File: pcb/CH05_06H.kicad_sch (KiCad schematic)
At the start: 10 parts

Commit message: Corrections to the coax driver
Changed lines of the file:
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@@
     (effects (font (size 1.27 1.27)) (justify right))
   )
-  (symbol (lib_id "Device:R") (at 96.52 52.07 270)
+  (symbol (lib_id "Device:R") (at 96.52 52.07 270) (unit 1)
     (in_bom yes) (on_board yes)
     (property "Reference" "R?" (id 0) (at 96.52 46.8122 90))
@@
     (pin "2")
   )
-  (symbol (lib_id "Device:R") (at 115.57 69.85 0)
+  (symbol (lib_id "Device:R") (at 115.57 69.85 0) (unit 1)
     (in_bom yes) (on_board yes)
     (property "Reference" "R?" (id 0) (at 117.348 68.6816 0)
@@
     (pin "2")
   )
-  (symbol (lib_id "power:GND") (at 115.57 87.63 0)
+  (symbol (lib_id "power:GND") (at 115.57 87.63 0) (unit 1)
     (in_bom yes) (on_board yes)
     (property "Reference" "#PWR?" (id 0) (at 115.57 93.98 0)
@@
     (pin "1")
   )
-  (symbol (lib_id "Device:R") (at 115.57 82.55 0)
+  (symbol (lib_id "Device:R") (at 115.57 82.55 0) (unit 1)
     (in_bom yes) (on_board yes)
     (property "Reference" "R?" (id 0) (at 117.348 81.3816 0)
@@
     (pin "2")
   )
-  (symbol (lib_id "Device:R") (at 115.57 135.89 0)
+  (symbol (lib_id "Device:R") (at 115.57 135.89 0) (unit 1)
     (in_bom yes) (on_board yes)
     (property "Reference" "R?" (id 0) (at 117.348 134.7216 0)
@@
     (pin "2")
   )
-  (symbol (lib_id "power:GND") (at 115.57 154.94 0)
+  (symbol (lib_id "power:GND") (at 115.57 154.94 0) (unit 1)
     (in_bom yes) (on_board yes)
     (property "Reference" "#PWR?" (id 0) (at 115.57 161.29 0)
@@
     (pin "1")
   )
-  (symbol (lib_id "Device:R") (at 115.57 148.59 0)
+  (symbol (lib_id "Device:R") (at 115.57 148.59 0) (unit 1)
     (in_bom yes) (on_board yes)
     (property "Reference" "R?" (id 0) (at 117.348 147.4216 0)
@@
     (pin "2")
   )
-  (symbol (lib_id "Connector:Conn_Coaxial") (at 115.57 59.69 0)
+  (symbol (lib_id "Connector:Conn_Coaxial") (at 115.57 59.69 0) (unit 1)
     (in_bom yes) (on_board yes)
     (property "Reference" "J?" (id 0) (at 118.11 60.325 0)
@@
     (pin "2")
   )
-  (symbol (lib_id "Connector:Conn_Coaxial") (at 115.57 125.73 0)
+  (symbol (lib_id "Connector:Conn_Coaxial") (at 115.57 125.73 0) (unit 1)
     (in_bom yes) (on_board yes)
     (property "Reference" "J?" (id 0) (at 118.11 126.365 0)
@@
     (pin "2")
   )
-  (symbol (lib_id "Device:R") (at 93.98 118.11 270)
+  (symbol (lib_id "Device:R") (at 93.98 118.11 270) (unit 1)
     (in_bom yes) (on_board yes)
     (property "Reference" "R?" (id 0) (at 93.98 112.8522 90))
@@
     (pin "2")
   )
-  (symbol (lib_id "Transistor_BJT:BC856BS") (at 106.68 118.11 0) (mirror x)
+  (symbol (lib_id "Transistor_BJT:BC856BS") (at 106.68 118.11 0) (mirror x) (unit 1)
     (in_bom yes) (on_board yes)
     (property "Reference" "Q?" (id 0) (at 111.506 119.2784 0)
@@
       (effects (font (size 1.27 1.27)) hide)
     )
-    (pin "3")
-    (pin "4")
-    (pin "5")
+    (pin "1")
+    (pin "2")
+    (pin "6")
   )
-  (symbol (lib_id "Transistor_BJT:BC856BS") (at 106.68 52.07 0) (mirror x)
+  (symbol (lib_id "Transistor_BJT:BC856BS") (at 106.68 52.07 0) (mirror x) (unit 1)
     (in_bom yes) (on_board yes)
     (property "Reference" "Q?" (id 0) (at 111.506 53.2384 0)

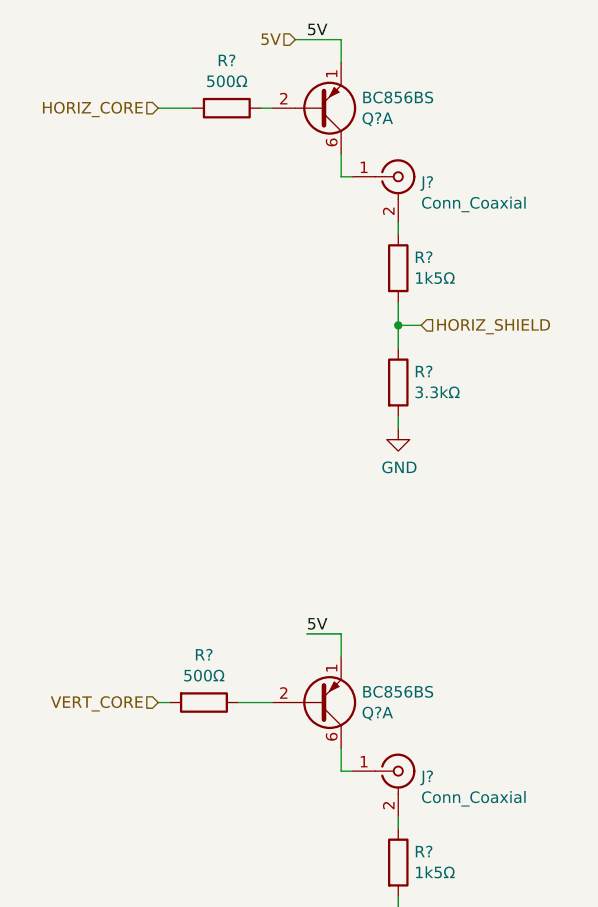
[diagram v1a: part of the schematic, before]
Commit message: Shift register updates - changes the driver from pnp to npn
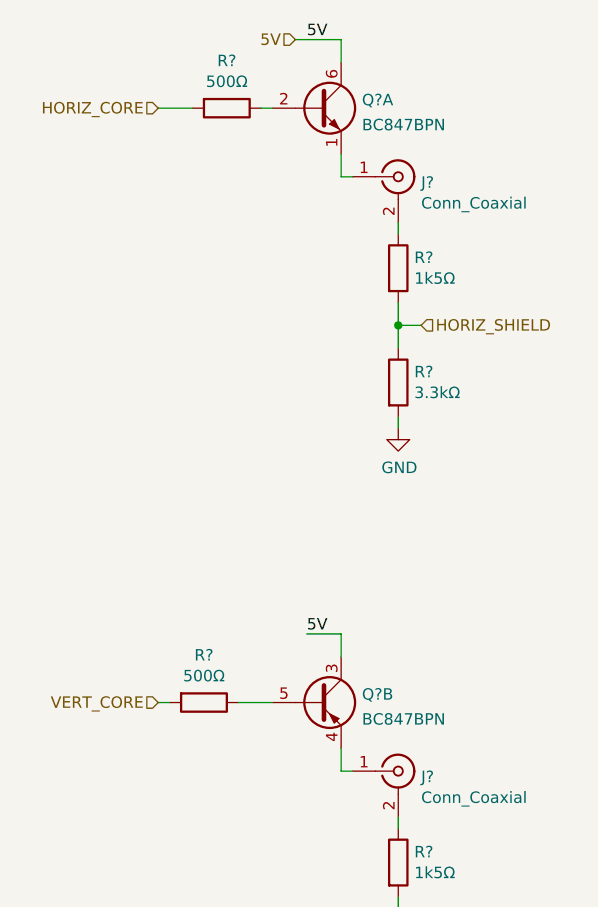
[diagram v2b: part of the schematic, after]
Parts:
- removed Q? (x2): BC856BS, Package_TO_SOT_SMD:SOT-363_SC-70-6, symbol Transistor_BJT:BC856BS
- added Q? (x2): BC847BPN, Package_TO_SOT_SMD:SOT-363_SC-70-6, symbol Transistor_BJT:BC847BPN
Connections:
- net 5V: now also Q?.3 (C2), Q?.6 (C1)
- net at R?.1: now also Q?.2 (B1)
- net at J?.1 (In): now also Q?.1 (E1)
- net at J?.1 (In): now also Q?.4 (E2)
- net at R?.1: now also Q?.5 (B2)
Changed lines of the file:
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@@
     (pin "2")
   )
-  (symbol (lib_id "Transistor_BJT:BC856BS") (at 106.68 118.11 0) (mirror x) (unit 1)
-    (in_bom yes) (on_board yes)
-    (property "Reference" "Q?" (id 0) (at 111.506 119.2784 0)
+  (symbol (lib_id "Transistor_BJT:BC847BPN") (at 106.68 118.11 0) (unit 2)
+    (in_bom yes) (on_board yes) (fields_autoplaced)
+    (property "Reference" "Q?" (id 0) (at 111.5314 117.2015 0)
       (effects (font (size 1.27 1.27)) (justify left))
     )
-    (property "Value" "BC856BS" (id 1) (at 111.506 116.967 0)
+    (property "Value" "BC847BPN" (id 1) (at 111.5314 119.9766 0)
       (effects (font (size 1.27 1.27)) (justify left))
     )
-    (property "Footprint" "Package_TO_SOT_SMD:SOT-363_SC-70-6" (id 2) (at 111.76 120.65 0)
+    (property "Footprint" "Package_TO_SOT_SMD:SOT-363_SC-70-6" (id 2) (at 111.76 115.57 0)
       (effects (font (size 1.27 1.27)) hide)
     )
-    (property "Datasheet" "https://assets.nexperia.com/documents/data-sheet/BC856BS.pdf" (id 3) (at 106.68 118.11 0)
+    (property "Datasheet" "https://assets.nexperia.com/documents/data-sheet/BC847BPN.pdf" (id 3) (at 106.68 118.11 0)
       (effects (font (size 1.27 1.27)) hide)
     )
-    (pin "1")
-    (pin "2")
-    (pin "6")
+    (pin "3")
+    (pin "4")
+    (pin "5")
   )
-  (symbol (lib_id "Transistor_BJT:BC856BS") (at 106.68 52.07 0) (mirror x) (unit 1)
-    (in_bom yes) (on_board yes)
-    (property "Reference" "Q?" (id 0) (at 111.506 53.2384 0)
+  (symbol (lib_id "Transistor_BJT:BC847BPN") (at 106.68 52.07 0) (unit 1)
+    (in_bom yes) (on_board yes) (fields_autoplaced)
+    (property "Reference" "Q?" (id 0) (at 111.5314 51.1615 0)
       (effects (font (size 1.27 1.27)) (justify left))
     )
-    (property "Value" "BC856BS" (id 1) (at 111.506 50.927 0)
+    (property "Value" "BC847BPN" (id 1) (at 111.5314 53.9366 0)
       (effects (font (size 1.27 1.27)) (justify left))
     )
-    (property "Footprint" "Package_TO_SOT_SMD:SOT-363_SC-70-6" (id 2) (at 111.76 54.61 0)
+    (property "Footprint" "Package_TO_SOT_SMD:SOT-363_SC-70-6" (id 2) (at 111.76 49.53 0)
       (effects (font (size 1.27 1.27)) hide)
     )
-    (property "Datasheet" "https://assets.nexperia.com/documents/data-sheet/BC856BS.pdf" (id 3) (at 106.68 52.07 0)
+    (property "Datasheet" "https://assets.nexperia.com/documents/data-sheet/BC847BPN.pdf" (id 3) (at 106.68 52.07 0)
       (effects (font (size 1.27 1.27)) hide)
     )

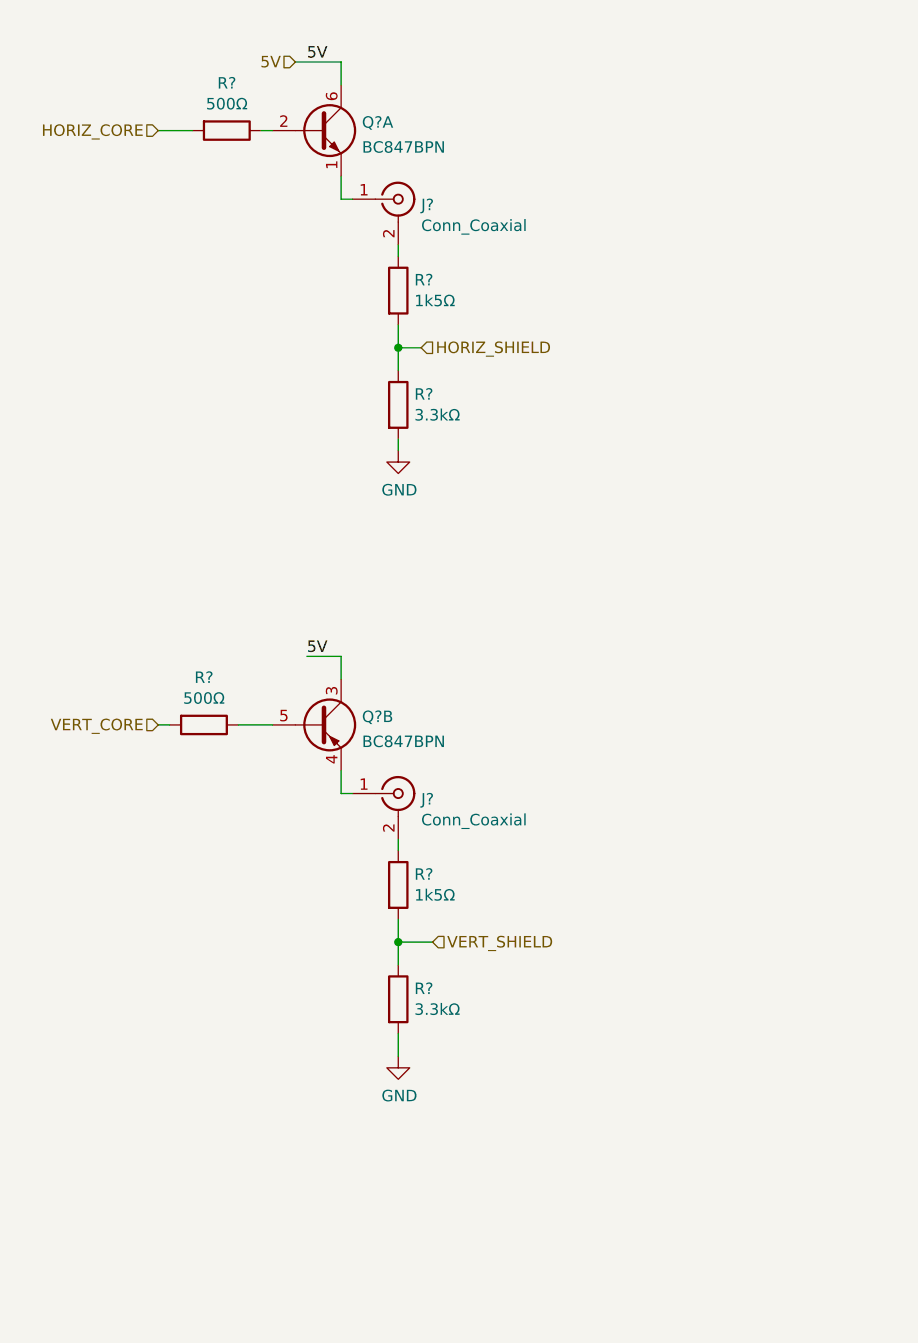
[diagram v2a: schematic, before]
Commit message: Adds line protection
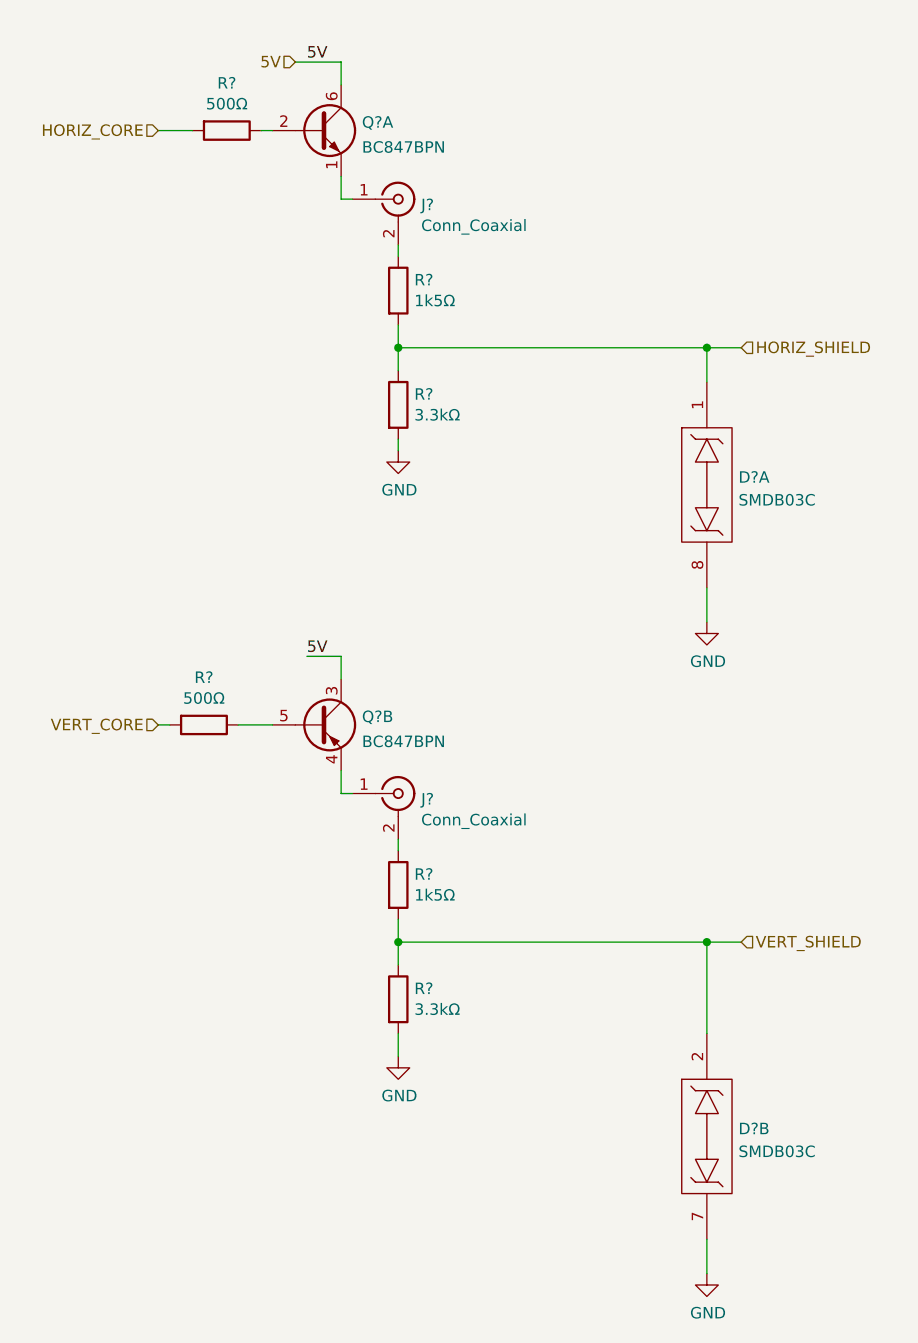
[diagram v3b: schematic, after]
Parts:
- added D? (x2): SMDB03C, Package_SO:SO-8_3.9x4.9mm_P1.27mm, symbol CoaxTester:SMDB03C
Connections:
- net GND: now also D?.7, D?.8
- net HORIZ_SHIELD: now also D?.1
- net VERT_SHIELD: now also D?.2
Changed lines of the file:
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@@
   (junction (at 115.57 76.2) (diameter 0) (color 0 0 0 0)
   )
+  (junction (at 149.86 76.2) (diameter 0) (color 0 0 0 0)
+  )
   (junction (at 115.57 142.24) (diameter 0) (color 0 0 0 0)
   )
+  (junction (at 149.86 142.24) (diameter 0) (color 0 0 0 0)
+  )
   (wire (pts (xy 88.9 118.11) (xy 90.17 118.11))
     (stroke (width 0) (type default) (color 0 0 0 0))
@@
     (stroke (width 0) (type default) (color 0 0 0 0))
   )
-  (wire (pts (xy 115.57 76.2) (xy 118.11 76.2))
+  (wire (pts (xy 115.57 76.2) (xy 149.86 76.2))
     (stroke (width 0) (type default) (color 0 0 0 0))
   )
@@
     (stroke (width 0) (type default) (color 0 0 0 0))
   )
+  (wire (pts (xy 149.86 102.87) (xy 149.86 106.68))
+    (stroke (width 0) (type default) (color 0 0 0 0))
+  )
   (wire (pts (xy 109.22 59.69) (xy 110.49 59.69))
     (stroke (width 0) (type default) (color 0 0 0 0))
@@
     (stroke (width 0) (type default) (color 0 0 0 0))
   )
+  (wire (pts (xy 115.57 142.24) (xy 149.86 142.24))
+    (stroke (width 0) (type default) (color 0 0 0 0))
+  )
   (wire (pts (xy 109.22 110.49) (xy 105.41 110.49))
     (stroke (width 0) (type default) (color 0 0 0 0))
@@
     (stroke (width 0) (type default) (color 0 0 0 0))
   )
+  (wire (pts (xy 149.86 76.2) (xy 153.67 76.2))
+    (stroke (width 0) (type default) (color 0 0 0 0))
+  )
+  (wire (pts (xy 149.86 76.2) (xy 149.86 80.01))
+    (stroke (width 0) (type default) (color 0 0 0 0))
+  )
   (wire (pts (xy 88.9 52.07) (xy 92.71 52.07))
     (stroke (width 0) (type default) (color 0 0 0 0))
@@
     (stroke (width 0) (type default) (color 0 0 0 0))
   )
+  (wire (pts (xy 149.86 142.24) (xy 153.67 142.24))
+    (stroke (width 0) (type default) (color 0 0 0 0))
+  )
+  (wire (pts (xy 149.86 175.26) (xy 149.86 179.07))
+    (stroke (width 0) (type default) (color 0 0 0 0))
+  )
   (wire (pts (xy 100.33 52.07) (xy 101.6 52.07))
     (stroke (width 0) (type default) (color 0 0 0 0))
@@
     (stroke (width 0) (type default) (color 0 0 0 0))
   )
-  (wire (pts (xy 115.57 142.24) (xy 119.38 142.24))
+  (wire (pts (xy 149.86 142.24) (xy 149.86 152.4))
     (stroke (width 0) (type default) (color 0 0 0 0))
   )
@@
     (effects (font (size 1.27 1.27)) (justify left bottom))
   )
-  (hierarchical_label "HORIZ_SHIELD" (shape input) (at 118.11 76.2 0)
+  (hierarchical_label "HORIZ_SHIELD" (shape input) (at 153.67 76.2 0)
     (effects (font (size 1.27 1.27)) (justify left))
   )
@@
     (effects (font (size 1.27 1.27)) (justify right))
   )
-  (hierarchical_label "VERT_SHIELD" (shape input) (at 119.38 142.24 0)
+  (hierarchical_label "VERT_SHIELD" (shape input) (at 153.67 142.24 0)
     (effects (font (size 1.27 1.27)) (justify left))
   )
@@
     (pin "5")
   )
+  (symbol (lib_id "power:GND") (at 149.86 179.07 0) (unit 1)
+    (in_bom yes) (on_board yes)
+    (property "Reference" "#PWR?" (id 0) (at 149.86 185.42 0)
+      (effects (font (size 1.27 1.27)) hide)
+    )
+    (property "Value" "GND" (id 1) (at 149.987 183.4642 0))
+    (property "Footprint" "" (id 2) (at 149.86 179.07 0)
+      (effects (font (size 1.27 1.27)) hide)
+    )
+    (property "Datasheet" "" (id 3) (at 149.86 179.07 0)
+      (effects (font (size 1.27 1.27)) hide)
+    )
+    (pin "1")
+  )
+  (symbol (lib_id "CoaxTester:SMDB03C") (at 149.86 91.44 0) (unit 1)
+    (in_bom yes) (on_board yes) (fields_autoplaced)
+    (property "Reference" "D?" (id 0) (at 153.3652 90.6053 0)
+      (effects (font (size 1.27 1.27)) (justify left))
+    )
+    (property "Value" "SMDB03C" (id 1) (at 153.3652 93.1422 0)
+      (effects (font (size 1.27 1.27)) (justify left))
+    )
+    (property "Footprint" "Package_SO:SO-8_3.9x4.9mm_P1.27mm" (id 2) (at 149.86 90.17 0)
+      (effects (font (size 1.27 1.27)) hide)
+    )
+    (property "Datasheet" "https://www.smc-diodes.com/propdf/SMDB03C%20THRU%20SMDB24C%20N0426%20REV.A.pdf" (id 3) (at 149.86 90.17 0)
+      (effects (font (size 1.27 1.27)) hide)
+    )
+    (pin "1")
+    (pin "8")
+  )
+  (symbol (lib_id "CoaxTester:SMDB03C") (at 149.86 163.83 0) (unit 2)
+    (in_bom yes) (on_board yes) (fields_autoplaced)
+    (property "Reference" "D?" (id 0) (at 153.3652 162.9953 0)
+      (effects (font (size 1.27 1.27)) (justify left))
+    )
+    (property "Value" "SMDB03C" (id 1) (at 153.3652 165.5322 0)
+      (effects (font (size 1.27 1.27)) (justify left))
+    )
+    (property "Footprint" "Package_SO:SO-8_3.9x4.9mm_P1.27mm" (id 2) (at 149.86 162.56 0)
+      (effects (font (size 1.27 1.27)) hide)
+    )
+    (property "Datasheet" "https://www.smc-diodes.com/propdf/SMDB03C%20THRU%20SMDB24C%20N0426%20REV.A.pdf" (id 3) (at 149.86 162.56 0)
+      (effects (font (size 1.27 1.27)) hide)
+    )
+    (pin "2")
+    (pin "7")
+  )
   (symbol (lib_id "Transistor_BJT:BC847BPN") (at 106.68 52.07 0) (unit 1)
     (in_bom yes) (on_board yes) (fields_autoplaced)
@@
     (pin "6")
   )
+  (symbol (lib_id "power:GND") (at 149.86 106.68 0) (unit 1)
+    (in_bom yes) (on_board yes)
+    (property "Reference" "#PWR?" (id 0) (at 149.86 113.03 0)
+      (effects (font (size 1.27 1.27)) hide)
+    )
+    (property "Value" "GND" (id 1) (at 149.987 111.0742 0))
+    (property "Footprint" "" (id 2) (at 149.86 106.68 0)
+      (effects (font (size 1.27 1.27)) hide)
+    )
+    (property "Datasheet" "" (id 3) (at 149.86 106.68 0)
+      (effects (font (size 1.27 1.27)) hide)
+    )
+    (pin "1")
+  )
 )
